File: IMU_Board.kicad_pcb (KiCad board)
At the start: 2 copper layers, 38 x 24 mm, 14 parts, among them J1 Conn_01x06_Male, U1 LSM6DSMTR, U3 BMM150

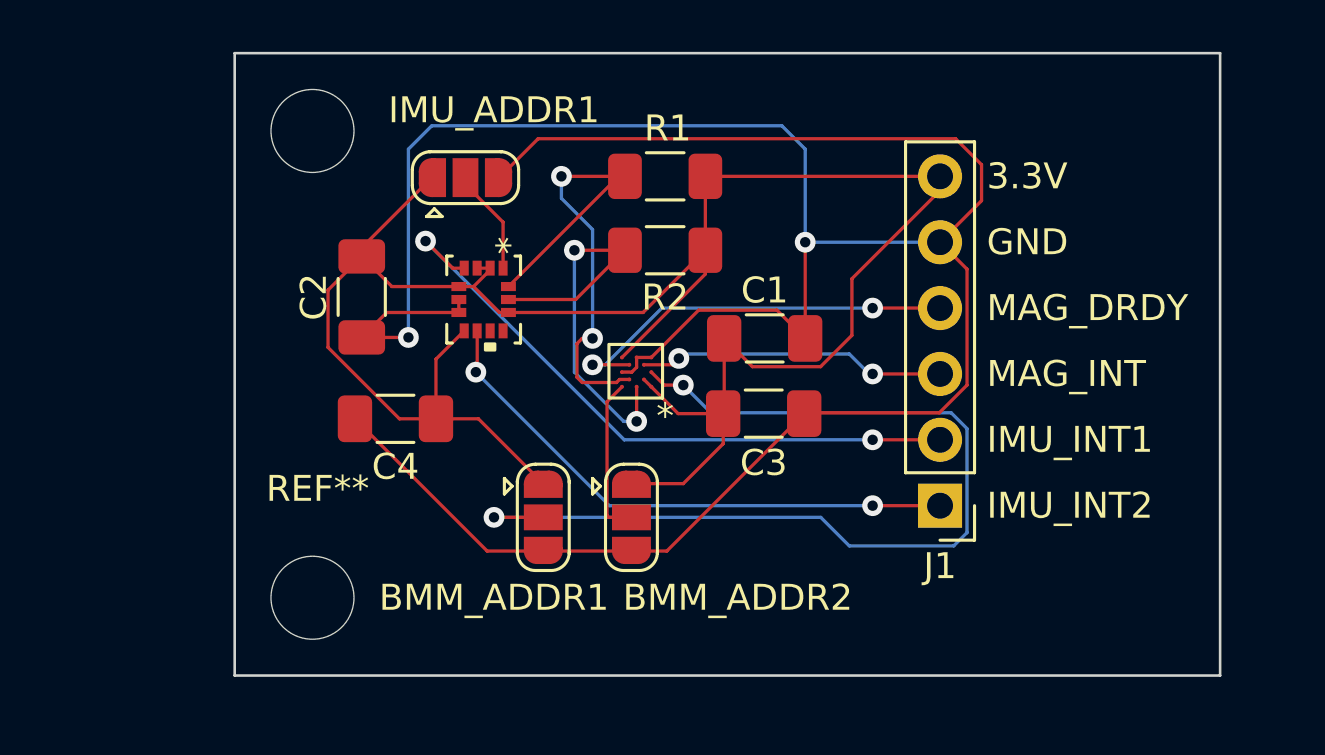
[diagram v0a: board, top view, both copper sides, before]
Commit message: v1.1 added resistors
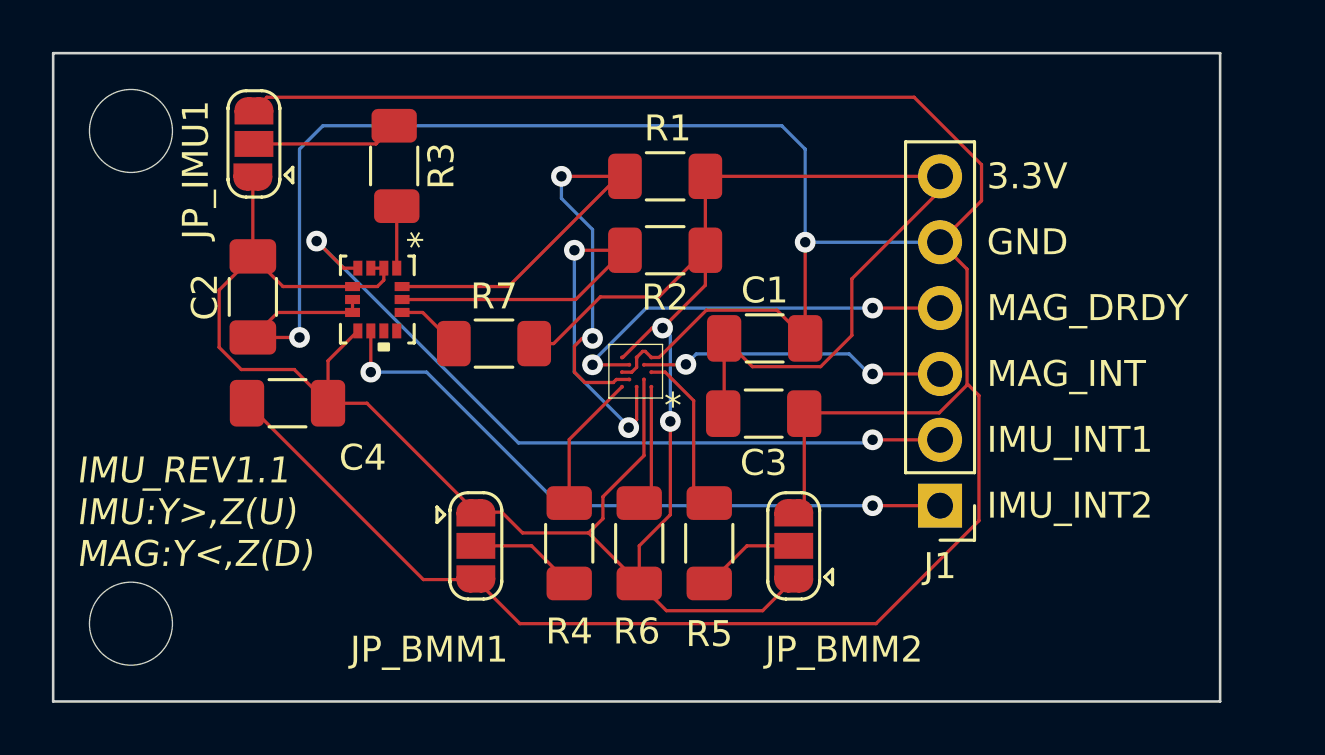
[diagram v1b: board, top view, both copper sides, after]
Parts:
- removed REF**: MountingHole_3.2mm_M3, MountingHole:MountingHole_3.2mm_M3
- added ?: , , F.Cu at (106.0, 109.0)
- added R3: 10K, Resistor_SMD:R_1206_3216Metric_Pad1.30x1.75mm_HandSolder, F.Cu at (116.2, 91.3)
- added R4: 10K, Resistor_SMD:R_1206_3216Metric_Pad1.30x1.75mm_HandSolder, F.Cu at (122.9, 105.9)
- added R5: 10K, Resistor_SMD:R_1206_3216Metric_Pad1.30x1.75mm_HandSolder, F.Cu at (128.3, 105.9)
- added R6: 10K, Resistor_SMD:R_1206_3216Metric_Pad1.30x1.75mm_HandSolder, F.Cu at (125.6, 105.9)
- added R7: 10K, Resistor_SMD:R_1206_3216Metric_Pad1.30x1.75mm_HandSolder, F.Cu at (120.0, 98.2)
- moved JP_BMM2 9.72 mm to (131.6, 106.0), turned to 90 degrees
- moved JP_IMU1 8.26 mm to (110.7, 90.5), turned to 90 degrees
- moved ? 7.00 mm to (106.0, 90.0), turned to -90 degrees
- moved JP_BMM1 6.10 mm to (119.3, 106.0)
- moved C4 4.21 mm to (112.0, 100.5)
- moved C2 4.20 mm to (110.7, 96.4)
- moved U1 4.10 mm to (115.5, 96.5)
- renumbered BMM_ADDR2 to JP_BMM1, BMM_ADDR1 to JP_BMM2, IMU_ADDR1 to JP_IMU1
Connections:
- U1 pad 1: Net-(JP_IMU1-Pad2) -> Net-(U1-Pad1)
- U1 pad 12: VCC -> Net-(U1-Pad12)
- U3 pad A1: VCC -> Net-(U3-PadA1)
- U3 pad A5: Net-(JP_BMM1-Pad2) -> Net-(U3-PadA5)
- U3 pad C1: Net-(JP_BMM2-Pad2) -> Net-(U3-PadC1)
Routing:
- net GND: track 109.0 -> 144.0 mm
- net Net-(JP_BMM2-Pad2): track 37.9 -> 3.86 mm, vias 2 -> 0
- net VCC: track 82.1 -> 103.1 mm, vias 0 -> 2
- net Net-(U3-PadC1): track 0.00 -> 6.29 mm
- net Net-(U3-PadA5): track 0.00 -> 5.33 mm
- net Net-(U3-PadA1): track 0.00 -> 4.68 mm
- net IMU_INT1: track 24.9 -> 29.2 mm
- net /SCL: track 16.5 -> 20.7 mm
- net IMU_INT2: track 21.6 -> 25.7 mm
- net /SDA: track 20.0 -> 23.7 mm
- net Net-(U1-Pad12): track 0.00 -> 2.49 mm
- net Net-(U1-Pad1): track 0.00 -> 2.39 mm
- net Net-(JP_BMM1-Pad2): track 6.17 -> 4.20 mm
- net Net-(JP_IMU1-Pad2): track 4.09 -> 5.70 mm
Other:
- board size 38 x 24 mm -> 45 x 25 mm
- rule pad_to_mask_clearance: 0.05 -> 0
- board text added: "IMU_REV1.1 IMU:Y>,Z(U) MAG:Y<,Z(D)"

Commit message: Silk Screen Adjustments
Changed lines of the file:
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@@
     (fp_line (start 1.6 -0.8) (end 1.6 0.8) (layer "F.Fab") (width 0.1))
     (fp_line (start 1.6 0.8) (end -1.6 0.8) (layer "F.Fab") (width 0.1))
-    (pad "1" smd roundrect (at -1.55 0) (size 1.3 1.75) (layers "F.Cu" "F.Paste" "F.Mask") (roundrect_rratio 0.192308)
+    (pad "1" smd roundrect (at -1.55 0) (size 1.3 1.75) (layers "F.Cu" "F.Paste" "F.Mask") (roundrect_rratio 0.1923076923)
       (net 18 "Net-(U1-Pad12)") (pintype "passive"))
-    (pad "2" smd roundrect (at 1.55 0) (size 1.3 1.75) (layers "F.Cu" "F.Paste" "F.Mask") (roundrect_rratio 0.192308)
+    (pad "2" smd roundrect (at 1.55 0) (size 1.3 1.75) (layers "F.Cu" "F.Paste" "F.Mask") (roundrect_rratio 0.1923076923)
       (net 6 "VCC") (pintype "passive"))
     (model "${KICAD6_3DMODEL_DIR}/Resistor_SMD.3dshapes/R_1206_3216Metric.wrl"
@@
     (fp_line (start -1.6 -0.8) (end 1.6 -0.8) (layer "F.Fab") (width 0.1))
     (fp_line (start -1.6 0.8) (end -1.6 -0.8) (layer "F.Fab") (width 0.1))
-    (pad "1" smd roundrect (at -1.55 0 90) (size 1.3 1.75) (layers "F.Cu" "F.Paste" "F.Mask") (roundrect_rratio 0.192308)
+    (pad "1" smd roundrect (at -1.55 0 90) (size 1.3 1.75) (layers "F.Cu" "F.Paste" "F.Mask") (roundrect_rratio 0.1923076923)
       (net 11 "Net-(JP_BMM1-Pad2)") (pintype "passive"))
-    (pad "2" smd roundrect (at 1.55 0 90) (size 1.3 1.75) (layers "F.Cu" "F.Paste" "F.Mask") (roundrect_rratio 0.192308)
+    (pad "2" smd roundrect (at 1.55 0 90) (size 1.3 1.75) (layers "F.Cu" "F.Paste" "F.Mask") (roundrect_rratio 0.1923076923)
       (net 15 "Net-(U3-PadA5)") (pintype "passive"))
     (model "${KICAD6_3DMODEL_DIR}/Resistor_SMD.3dshapes/R_1206_3216Metric.wrl"
@@
     (fp_line (start 1.6 0.8) (end -1.6 0.8) (layer "F.Fab") (width 0.1))
     (fp_line (start -1.6 0.8) (end -1.6 -0.8) (layer "F.Fab") (width 0.1))
-    (pad "1" smd roundrect (at -1.55 0 270) (size 1.3 1.75) (layers "F.Cu" "F.Paste" "F.Mask") (roundrect_rratio 0.192308)
+    (pad "1" smd roundrect (at -1.55 0 270) (size 1.3 1.75) (layers "F.Cu" "F.Paste" "F.Mask") (roundrect_rratio 0.1923076923)
       (net 13 "Net-(JP_IMU1-Pad2)") (pintype "passive"))
-    (pad "2" smd roundrect (at 1.55 -0.1 270) (size 1.3 1.75) (layers "F.Cu" "F.Paste" "F.Mask") (roundrect_rratio 0.192308)
+    (pad "2" smd roundrect (at 1.55 -0.1 270) (size 1.3 1.75) (layers "F.Cu" "F.Paste" "F.Mask") (roundrect_rratio 0.1923076923)
       (net 14 "Net-(U1-Pad1)") (pintype "passive"))
     (model "${KICAD6_3DMODEL_DIR}/Resistor_SMD.3dshapes/R_1206_3216Metric.wrl"
@@
     (fp_line (start -1.6 -0.8) (end 1.6 -0.8) (layer "F.Fab") (width 0.1))
     (fp_line (start -1.6 0.8) (end -1.6 -0.8) (layer "F.Fab") (width 0.1))
-    (pad "1" smd roundrect (at -1.55 0 270) (size 1.3 1.75) (layers "F.Cu" "F.Paste" "F.Mask") (roundrect_rratio 0.192308)
+    (pad "1" smd roundrect (at -1.55 0 270) (size 1.3 1.75) (layers "F.Cu" "F.Paste" "F.Mask") (roundrect_rratio 0.1923076923)
       (net 16 "Net-(U3-PadC1)") (pintype "passive"))
-    (pad "2" smd roundrect (at 1.55 0 270) (size 1.3 1.75) (layers "F.Cu" "F.Paste" "F.Mask") (roundrect_rratio 0.192308)
+    (pad "2" smd roundrect (at 1.55 0 270) (size 1.3 1.75) (layers "F.Cu" "F.Paste" "F.Mask") (roundrect_rratio 0.1923076923)
       (net 12 "Net-(JP_BMM2-Pad2)") (pintype "passive"))
     (model "${KICAD6_3DMODEL_DIR}/Resistor_SMD.3dshapes/R_1206_3216Metric.wrl"
@@
     (fp_line (start 1.6 0.8) (end -1.6 0.8) (layer "F.Fab") (width 0.1))
     (fp_line (start 1.6 -0.8) (end 1.6 0.8) (layer "F.Fab") (width 0.1))
-    (pad "1" smd roundrect (at -1.55 0 90) (size 1.3 1.75) (layers "F.Cu" "F.Paste" "F.Mask") (roundrect_rratio 0.192308)
+    (pad "1" smd roundrect (at -1.55 0 90) (size 1.3 1.75) (layers "F.Cu" "F.Paste" "F.Mask") (roundrect_rratio 0.1923076923)
       (net 6 "VCC") (pintype "passive"))
-    (pad "2" smd roundrect (at 1.55 0 90) (size 1.3 1.75) (layers "F.Cu" "F.Paste" "F.Mask") (roundrect_rratio 0.192308)
+    (pad "2" smd roundrect (at 1.55 0 90) (size 1.3 1.75) (layers "F.Cu" "F.Paste" "F.Mask") (roundrect_rratio 0.1923076923)
       (net 17 "Net-(U3-PadA1)") (pintype "passive"))
     (model "${KICAD6_3DMODEL_DIR}/Resistor_SMD.3dshapes/R_1206_3216Metric.wrl"

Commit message: rev1.2
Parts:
- J1: footprint Connector_PinHeader_2.54mm:PinHeader_1x06_P2.54mm_Vertical -> Connector_PinHeader_2.54mm:PinHeader_1x08_P2.54mm_Vertical
- moved J1 10.5 mm to (147.1, 108.0)
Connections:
- J1 pad 5: GND -> SDA
- J1 pad 6: VCC -> SCL
- R1 pad 2: /SDA -> SDA
- R2 pad 2: /SCL -> SCL
- U1 pad 13: /SCL -> SCL
- U1 pad 14: /SDA -> SDA
- U3 pad A3: /SCL -> SCL
- U3 pad B4: /SDA -> SDA
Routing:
- net SCL: track 0.00 -> 56.6 mm, vias 0 -> 2
- net SDA: track 0.00 -> 51.0 mm, vias 0 -> 2
- net GND: track 144.0 -> 180.5 mm, vias 2 -> 3
- net /SDA: track 23.7 -> 0.00 mm, vias 2 -> 0
- net /SCL: track 20.7 -> 0.00 mm, vias 2 -> 0
- net VCC: track 103.1 -> 114.5 mm
- net IMU_INT2: track 25.7 -> 37.0 mm, vias 2 -> 1
- net MAG_DRDY: track 15.8 -> 27.1 mm, vias 2 -> 1
- net IMU_INT1: track 29.2 -> 40.5 mm, vias 2 -> 1
- net MAG_INT: track 11.8 -> 22.9 mm, vias 2 -> 1
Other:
- board size 45 x 25 mm -> 47 x 25 mm
- board text added: "IMU_REV1.2 IMU:Y>,Z(U) MAG:Y<,Z(D)"
- board text added: "SCL"
- board text added: "SDA"
- board text removed: "IMU_REV1.1 IMU:Y>,Z(U) MAG:Y<,Z(D)"
